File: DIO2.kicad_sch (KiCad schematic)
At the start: 27 parts, among them J8 DIO-2, J8 GPIO-IN, J8 GPIO-OUT, U1 TLP627-2, U2 TLP627-2, U3 TLP627-2, U4 TLP627-2, U5 TLP627-2, U6 TLP627-2, U7 TLP627-2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

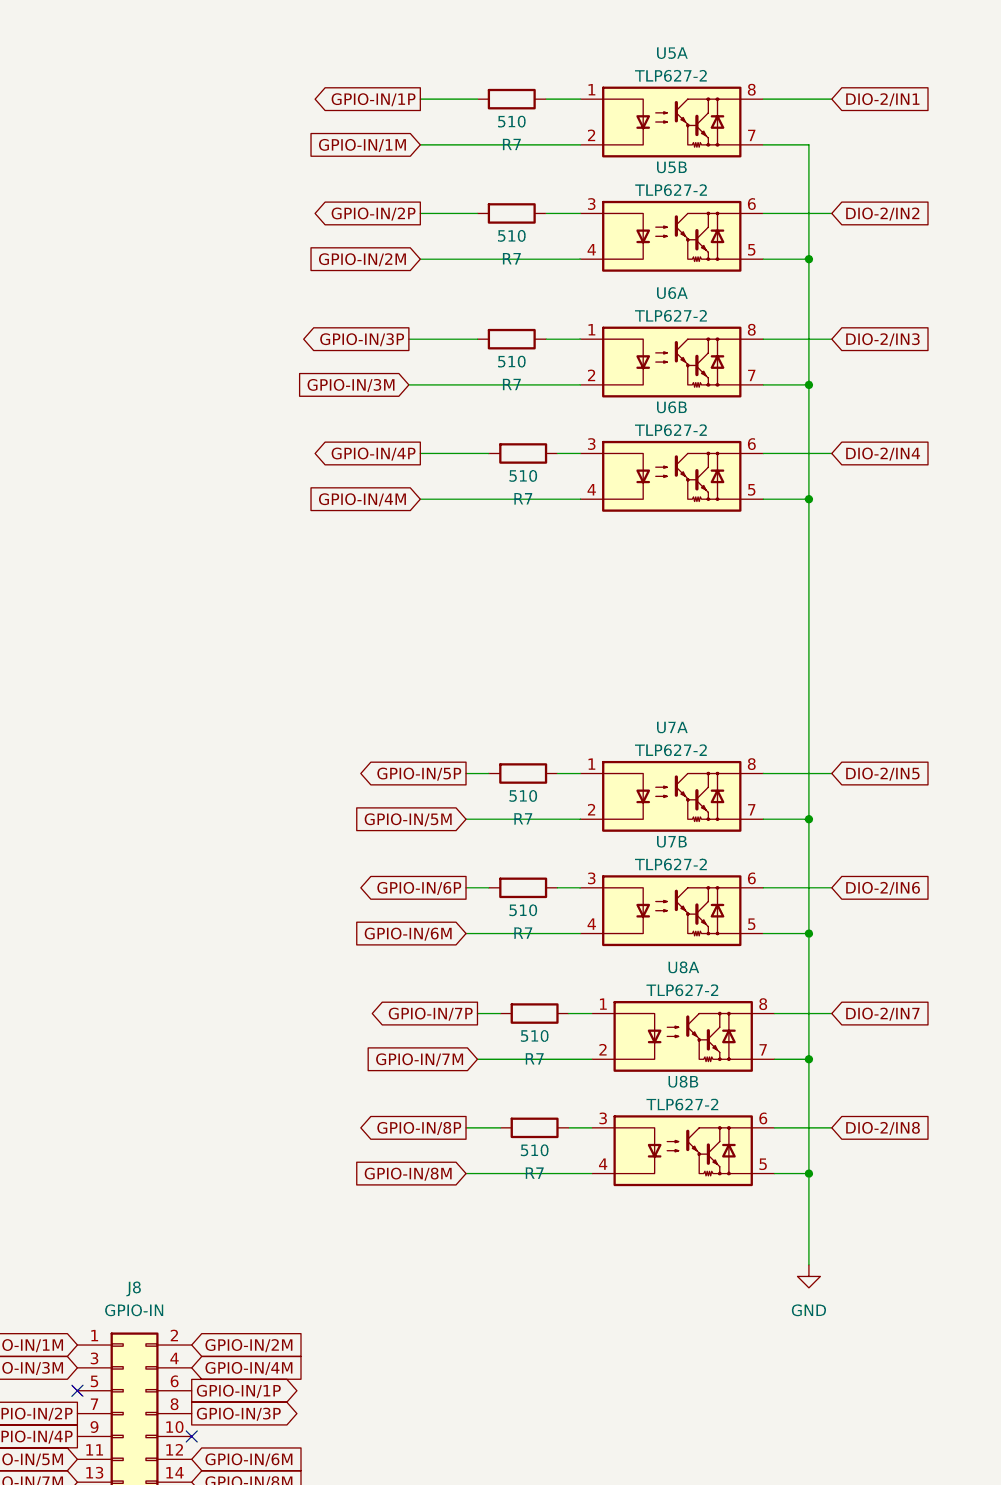
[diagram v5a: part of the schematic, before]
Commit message: bugfix GPIO/IN ドライ接点へ修正
GPIO/INはドライ接点
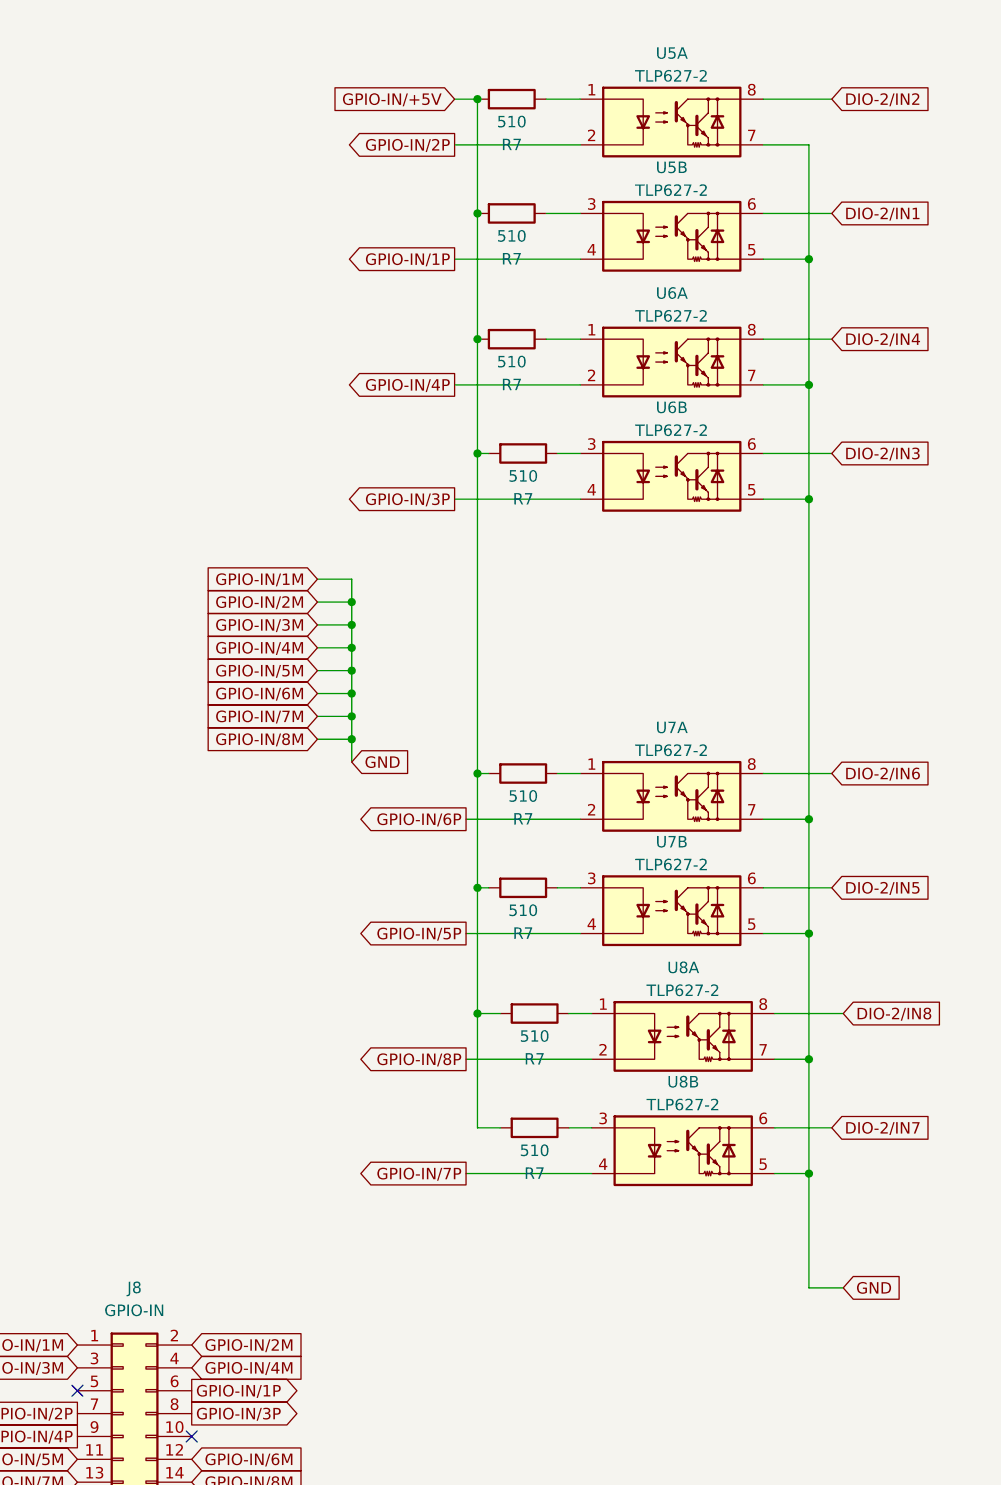
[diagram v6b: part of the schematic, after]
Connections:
- net DIO-2/IN1: now also U5.6; no longer U5.8
- net DIO-2/IN2: now also U5.8; no longer U5.6
- net DIO-2/IN3: now also U6.6; no longer U6.8
- net DIO-2/IN4: now also U6.8; no longer U6.6
- net DIO-2/IN5: now also U7.6; no longer U7.8
- net DIO-2/IN6: now also U7.8; no longer U7.6
- net DIO-2/IN7: now also U8.6; no longer U8.8
- net DIO-2/IN8: now also U8.8; no longer U8.6
- net GND: now also J8.1 (Pin_1), J8.11 (Pin_11), J8.12 (Pin_12), J8.13 (Pin_13), J8.14 (Pin_14), J8.2 (Pin_2), J8.3 (Pin_3), J8.4 (Pin_4)
- net GPIO-IN/1P: now also U5.4; no longer R7.2
- net GPIO-IN/2P: now also U5.2; no longer R7.2
- net GPIO-IN/3P: now also U6.4; no longer R7.2
- net GPIO-IN/4P: now also U6.2; no longer R7.2
- net GPIO-IN/5P: now also U7.4; no longer R7.2
- net GPIO-IN/6P: now also U7.2; no longer R7.2
- net GPIO-IN/7P: now also U8.4; no longer R7.2
- net GPIO-IN/8P: now also U8.2; no longer R7.2
- removed net GPIO-IN/1M: J8.1 (Pin_1), U5.2
- removed net GPIO-IN/2M: J8.2 (Pin_2), U5.4
- removed net GPIO-IN/3M: J8.3 (Pin_3), U6.2
- removed net GPIO-IN/4M: J8.4 (Pin_4), U6.4
- removed net GPIO-IN/5M: J8.11 (Pin_11), U7.2
- removed net GPIO-IN/6M: J8.12 (Pin_12), U7.4
- removed net GPIO-IN/7M: J8.13 (Pin_13), U8.2
- removed net GPIO-IN/8M: J8.14 (Pin_14), U8.4
- new net GPIO-IN/+5V: R7.2, R7.2, R7.2, R7.2, R7.2, R7.2, R7.2, R7.2
